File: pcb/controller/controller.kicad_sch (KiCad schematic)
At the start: 28 parts, among them J1 Conn_01x03, J2 Conn_01x03, J3 RELAY_CONN, J4 Remote_header, J5 PWR_IN, J6 MFRC_CONN, J7 Micro_SD_Card, Q1 MMBT3906, Q2 MMBT3906, Q3 IRLL014N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

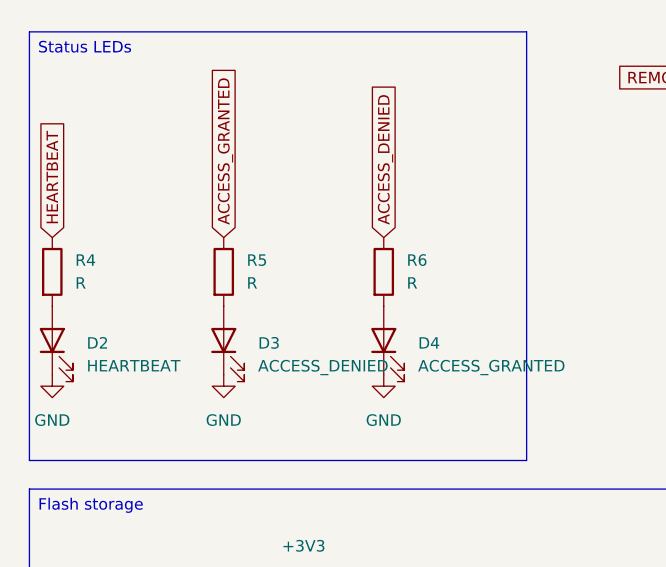
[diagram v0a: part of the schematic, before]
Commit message: Footprint updates Major restructuring
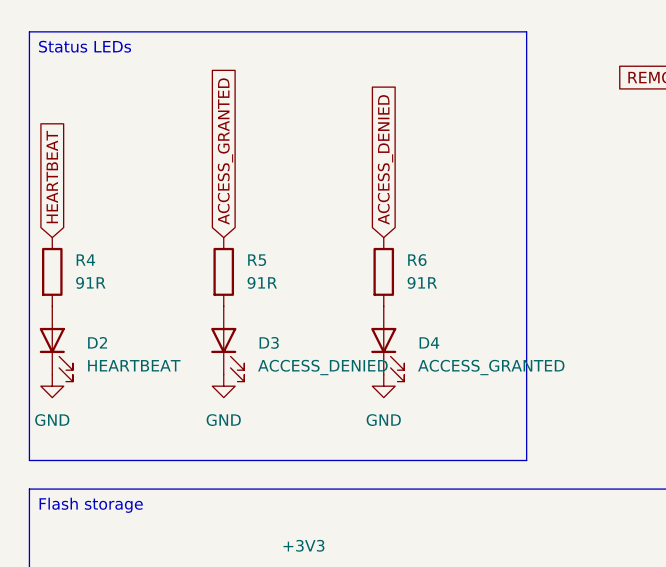
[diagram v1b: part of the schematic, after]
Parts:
- D1: footprint Diode_SMD:D_1206_3216Metric_Pad1.42x1.75mm_HandSolder -> Diode_SMD:D_SMA-SMB_Universal_Handsoldering
- R4, R5, R6: value R -> 91R
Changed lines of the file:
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@@
 			)
 		)
-		(property "Value" "R"
+		(property "Value" "91R"
 			(at 40.64 99.0599 0)
 			(effects
@@
 			)
 		)
-		(property "Footprint" "Diode_SMD:D_1206_3216Metric_Pad1.42x1.75mm_HandSolder"
+		(property "Footprint" "Diode_SMD:D_SMA-SMB_Universal_Handsoldering"
 			(at 93.98 34.29 0)
 			(effects
@@
 			)
 		)
-		(property "Value" "R"
+		(property "Value" "91R"
 			(at 58.42 99.0599 0)
 			(effects
@@
 			)
 		)
-		(property "Value" "R"
+		(property "Value" "91R"
 			(at 21.59 99.0599 0)
 			(effects

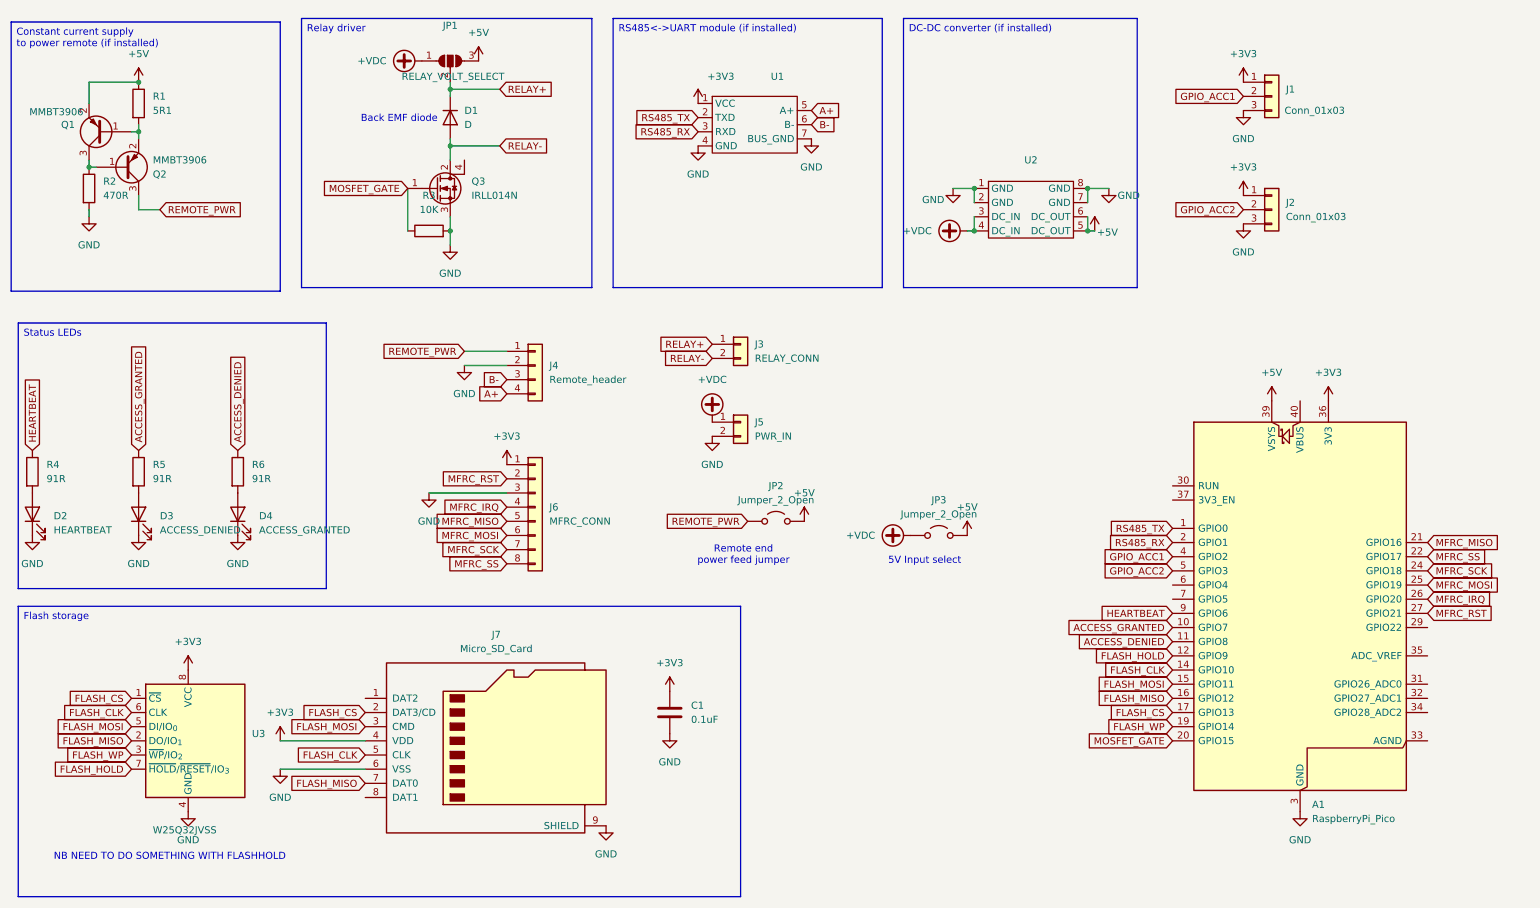
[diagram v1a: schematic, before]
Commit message: PCB changes - add GPIO3/4
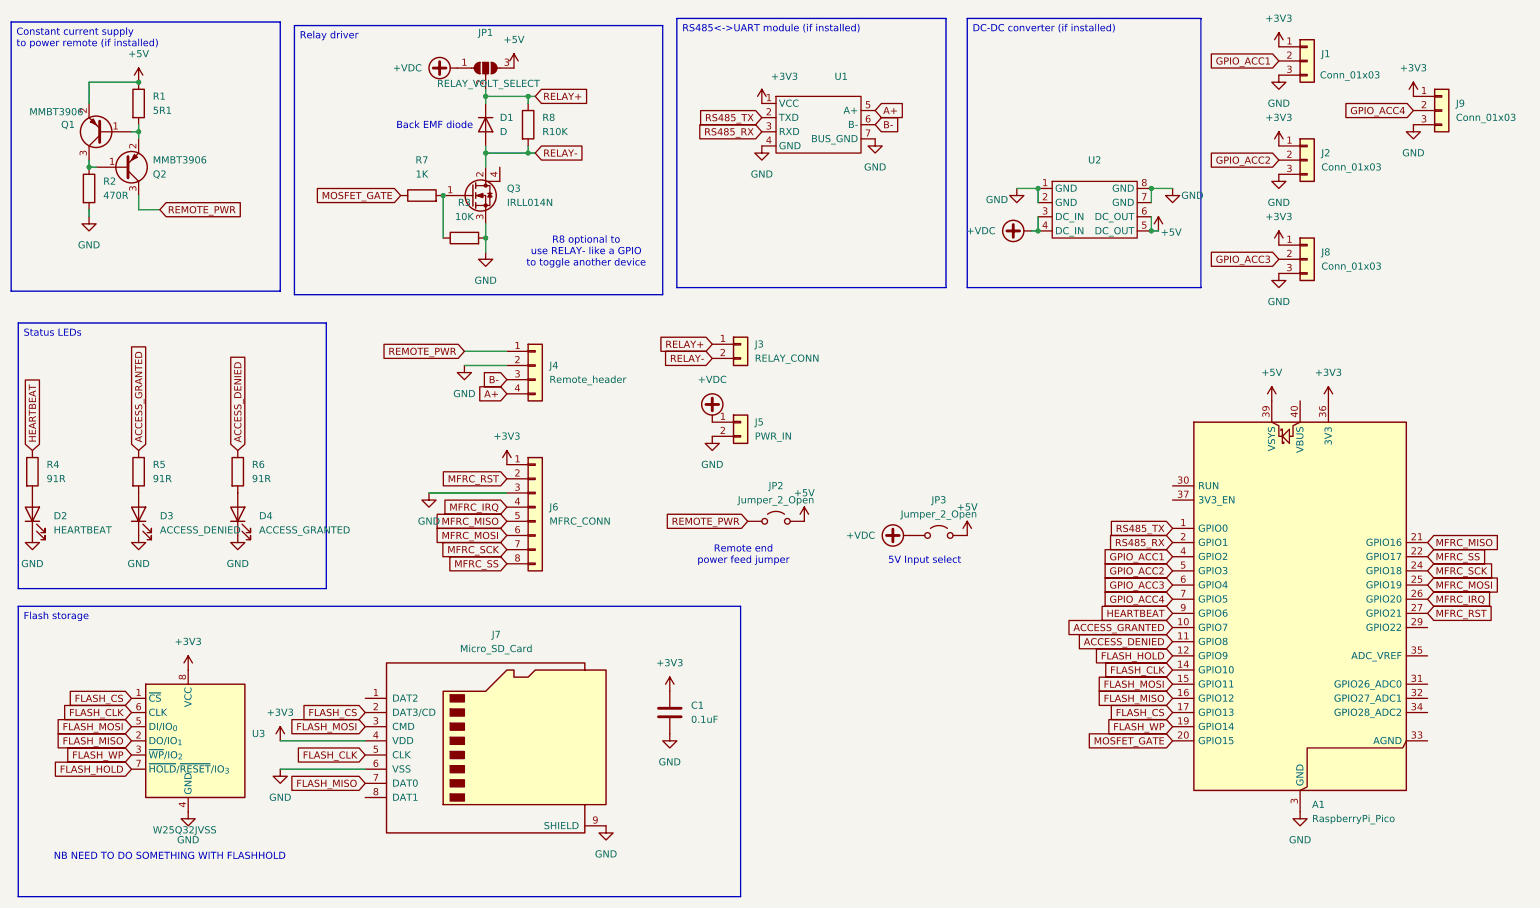
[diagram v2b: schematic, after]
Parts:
- added J8, J9: Conn_01x03, Connector_JST:JST_XH_B3B-XH-A_1x03_P2.50mm_Vertical, symbol Connector_Generic:Conn_01x03
- added R7: 1K, Resistor_SMD:R_1210_3225Metric_Pad1.30x2.65mm_HandSolder, symbol Device:R
- added R8: R10K, Resistor_SMD:R_1210_3225Metric_Pad1.30x2.65mm_HandSolder, symbol Device:R
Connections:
- net +3V3: now also J8.1 (Pin_1), J9.1 (Pin_1)
- net GND: now also J8.3 (Pin_3), J9.3 (Pin_3)
- net MOSFET_GATE: now also R7.1; no longer Q3.1 (G), R3.1
- net RELAY+: now also R8.1
- net RELAY-: now also R8.2
- net GPIO_ACC3: now reaches A1.6 (GPIO4)
- net GPIO_ACC3: now also J8.2 (Pin_2)
- net GPIO_ACC4: now reaches A1.7 (GPIO5)
- net GPIO_ACC4: now also J9.2 (Pin_2)
- new net: Q3.1 (G), R3.1, R7.2
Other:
- note added: "R8 optional to use RELAY- like a GPIO to toggle another device"
- moved on the sheet: D1, J1, J2, JP1, Q3, R3, U1, U2
